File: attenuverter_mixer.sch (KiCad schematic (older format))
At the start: 98 parts, among them J0 Eurorack power, J1 Input, J10 Or out, J2 Out, J3 Input, J4 Out, J5 Input, J6 Input, J7 Out, J8 Out, J9 Sum out, U1 TL072, U2 TL072, U3 TL072, U4 TL072, U5 TL074, U6 LM4040CIZ-5.0

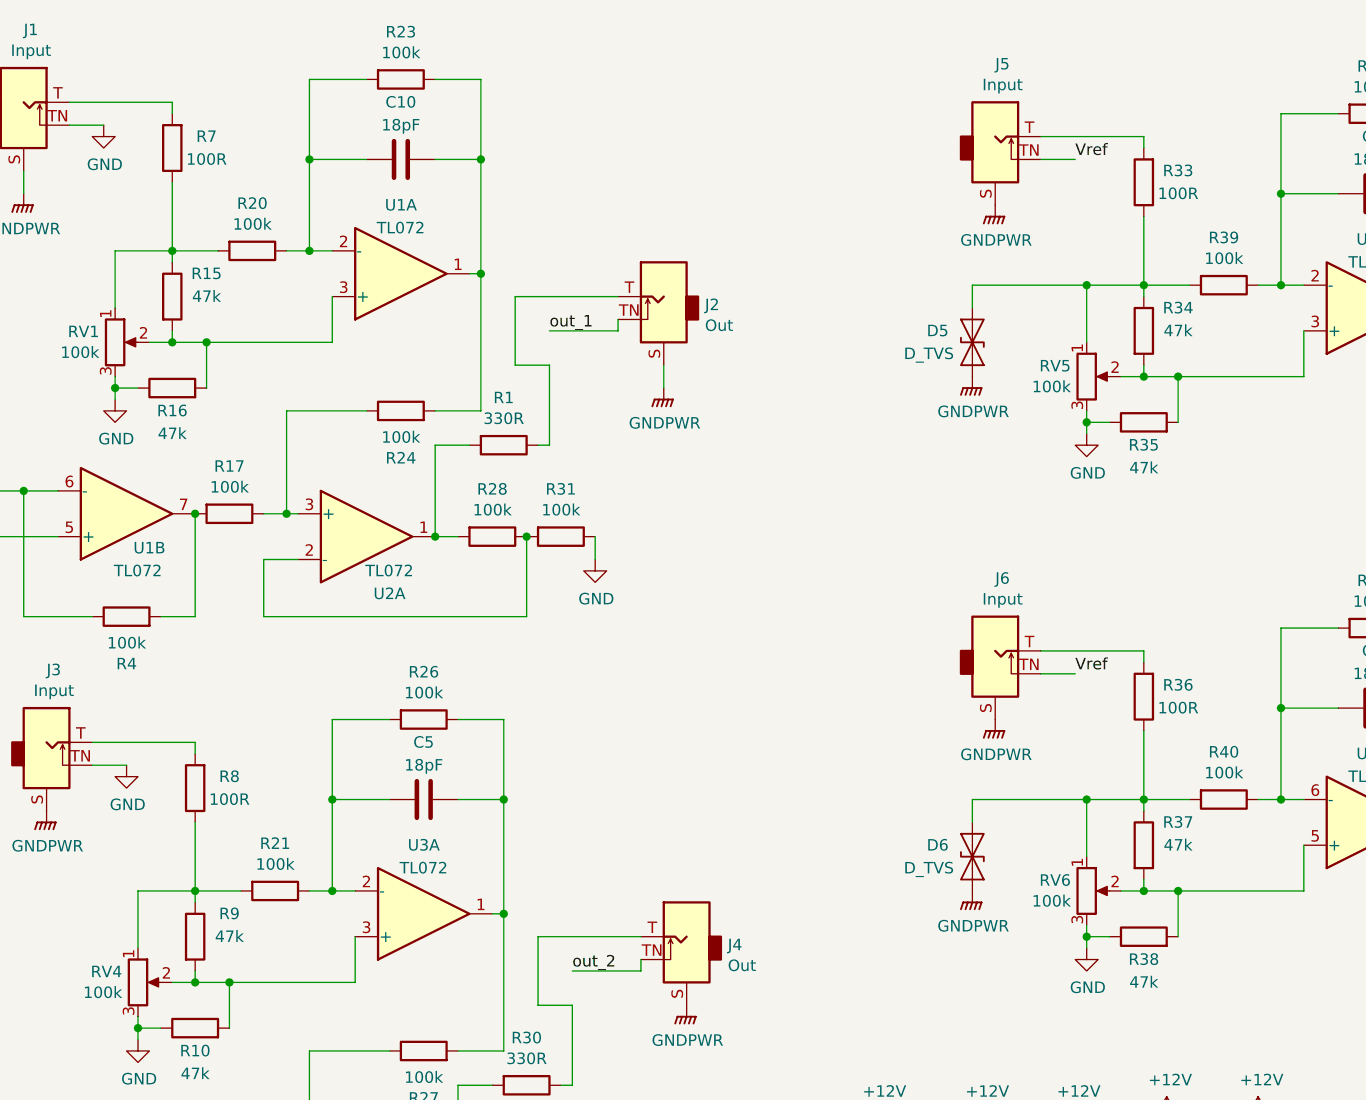
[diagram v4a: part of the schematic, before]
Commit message: remove two more TVS diodes; remove input resistors; use SM resistors
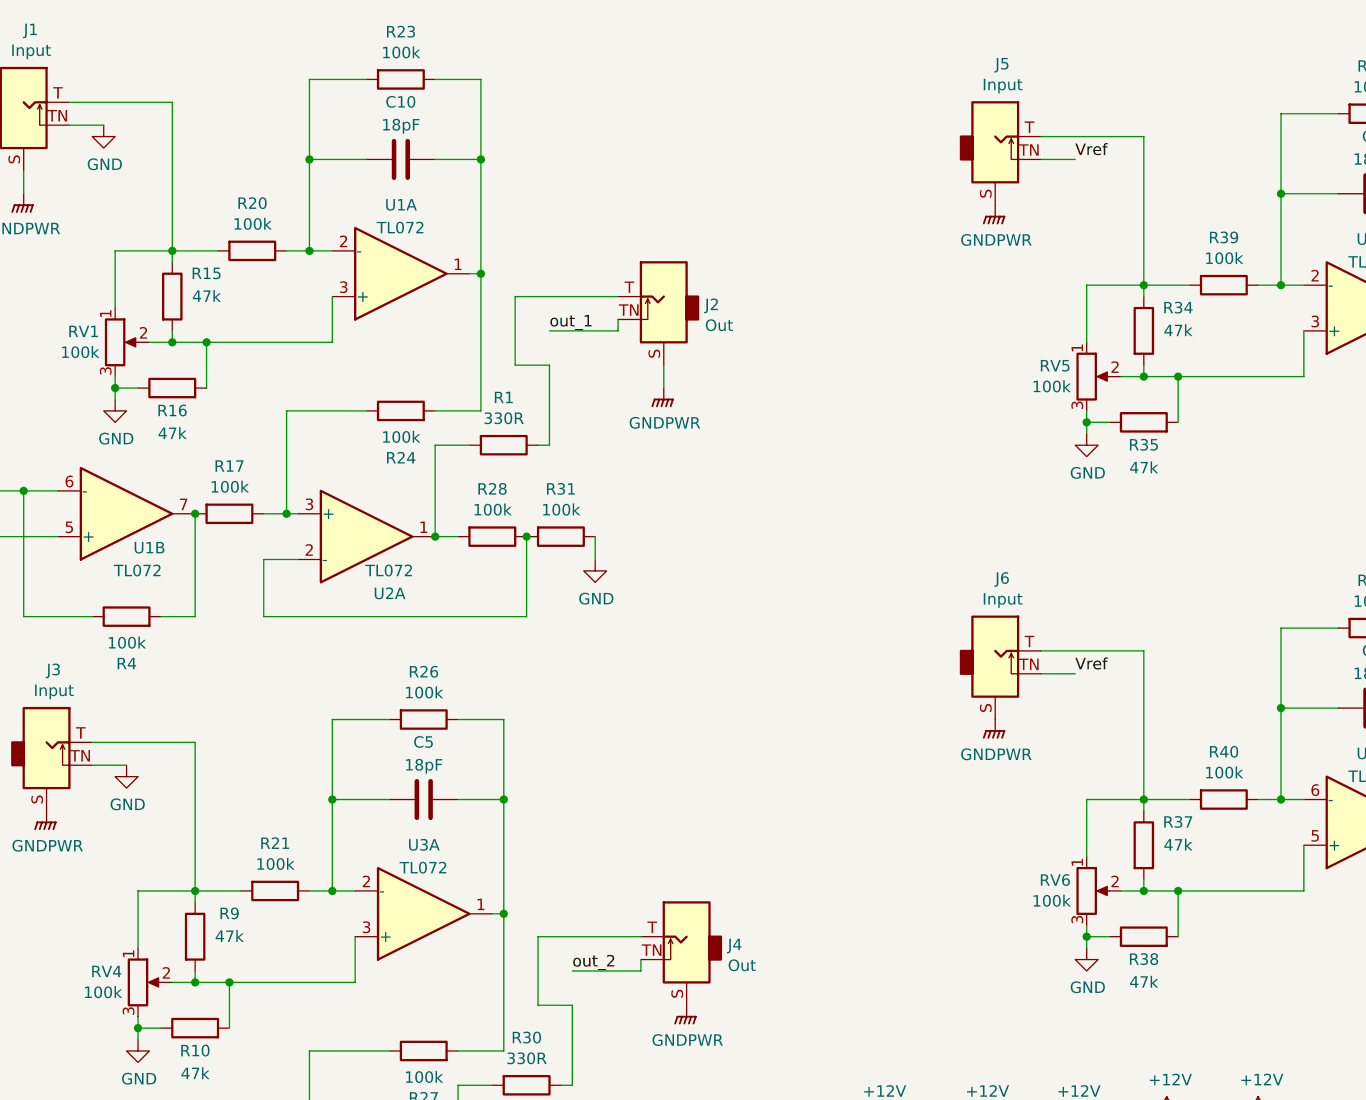
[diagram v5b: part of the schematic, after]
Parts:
- removed D5, D6: D_TVS, Diode_THT:D_DO-15_P12.70mm_Horizontal, symbol Device:D_TVS
- removed R33, R36, R7, R8: 100R, Resistor_THT:R_Axial_DIN0204_L3.6mm_D1.6mm_P7.62mm_Horizontal, symbol Device:R
- R10, R11, R12, R13, R14, R15, R16, R17, R18, R19, R2, R20, R21, R22, R23, R24, R25, R26, R27, R28, R29, R3, R34, R35, R37, R38, R39, R4, R40, R41, R42, R45, R46, R6, R9: footprint Resistor_THT:R_Axial_DIN0207_L6.3mm_D2.5mm_P10.16mm_Horizontal -> Resistor_SMD:R_1206_3216Metric_Pad1.42x1.75mm_HandSolder
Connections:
- net at J1.T: now also R15.1, R20.2, RV1.1
- net at J3.T: now also R21.2, R9.1, RV4.1
- net at J5.T: now also R34.1, R39.2, RV5.1
- net at J6.T: now also R37.1, R40.2, RV6.1

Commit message: Where it's at, just before changing the op amp configuration
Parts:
- J0: symbol Connector_Generic:Conn_02x05_Counter_Clockwise -> Connector_Generic:Conn_02x05_Odd_Even
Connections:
- net GND: now also J0.3 (Pin_3), J0.8 (Pin_8); no longer J0.2 (Pin_2), J0.9 (Pin_9)
- net GNDPWR: now also J0.5 (Pin_5), J0.6 (Pin_6); no longer J0.3 (Pin_3), J0.8 (Pin_8)
- net at D16.1 (K), J0.1 (Pin_1): now also J0.2 (Pin_2); no longer J0.10 (Pin_10)
- new net: D17.2 (A), J0.10 (Pin_10), J0.9 (Pin_9)
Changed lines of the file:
@@
 $EndComp
 $Comp
-L Connector_Generic:Conn_02x05_Counter_Clockwise J0
+L Connector_Generic:Conn_02x05_Odd_Even J0
 U 1 1 5DF894B6
 P 10050 1450

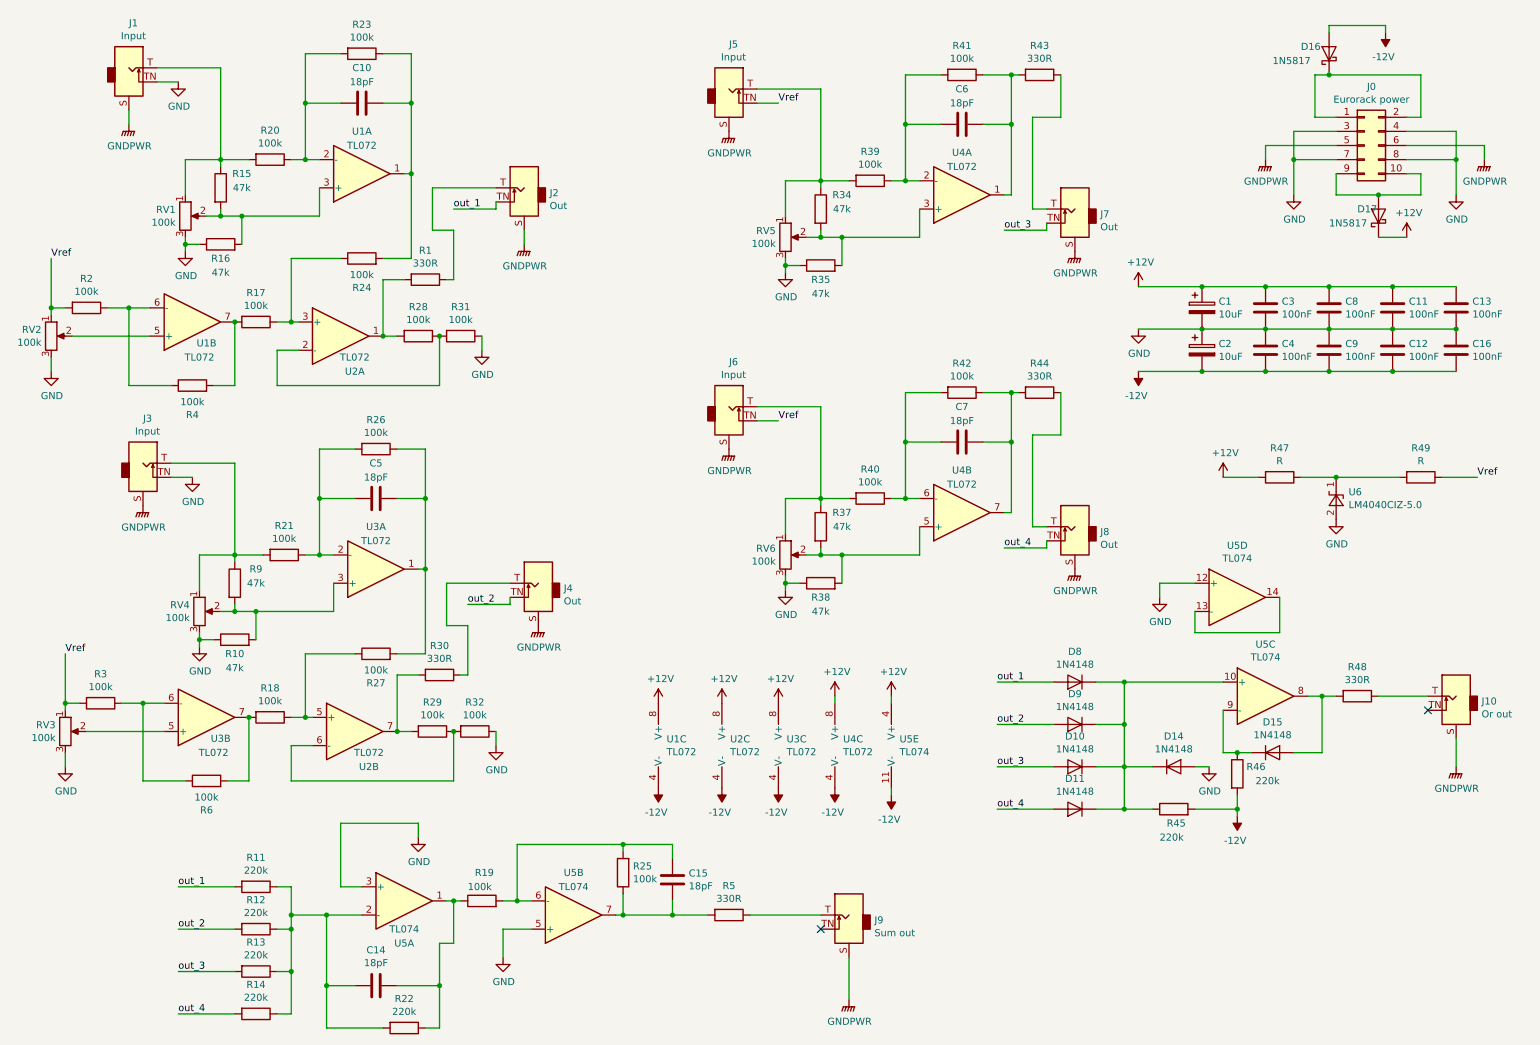
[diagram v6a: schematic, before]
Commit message: V01 as fabricated
- Use surface mount 100K and 220K to allow single board.
- Drop offset pots --- just have atteunuvert controls on each channel.
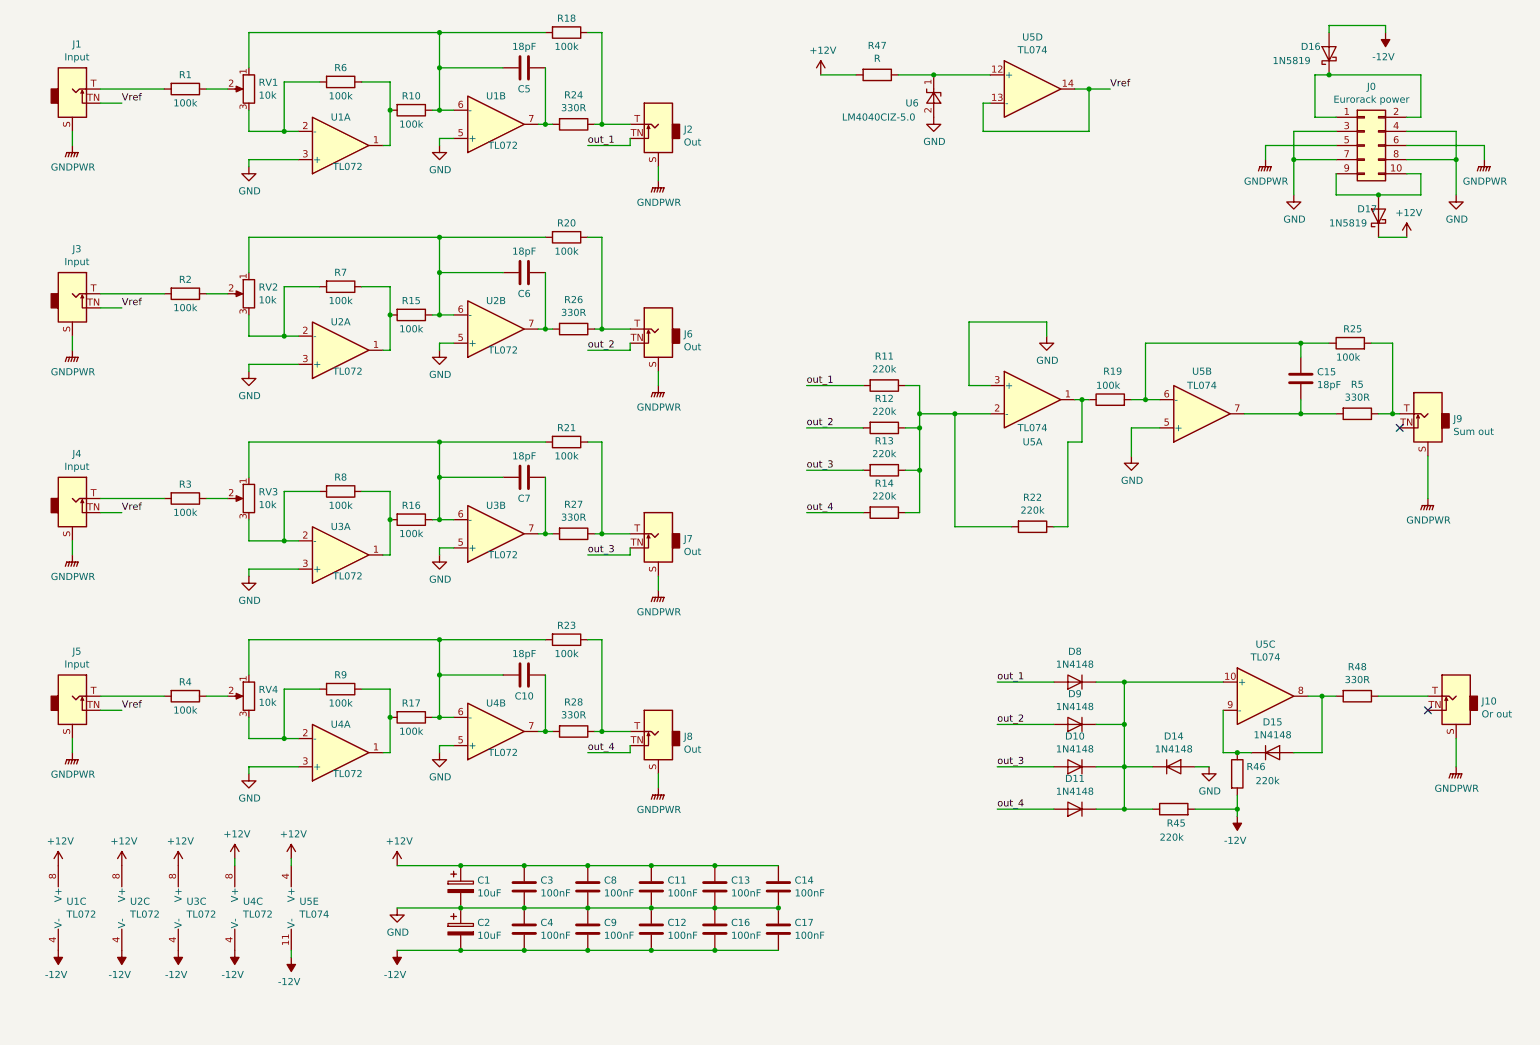
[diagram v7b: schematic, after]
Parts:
- removed R29, R39, R40, R41, R42: 100k, Resistor_SMD:R_1206_3216Metric_Pad1.42x1.75mm_HandSolder, symbol Device:R
- removed R30, R43, R44: 330R, Resistor_THT:R_Axial_DIN0309_L9.0mm_D3.2mm_P12.70mm_Horizontal, symbol Device:R
- removed R31, R32: 100k, Resistor_THT:R_Axial_DIN0207_L6.3mm_D2.5mm_P10.16mm_Horizontal, symbol Device:R
- removed R34, R35, R37, R38: 47k, Resistor_SMD:R_1206_3216Metric_Pad1.42x1.75mm_HandSolder, symbol Device:R
- removed R49: R, Resistor_THT:R_Axial_DIN0309_L9.0mm_D3.2mm_P12.70mm_Horizontal, symbol Device:R
- removed RV5, RV6: 100k, Potentiometer_THT:Potentiometer_Alpha_RD901F-40-00D_Single_Vertical, symbol Device:R_POT
- added C17: 100nF, Capacitor_THT:C_Disc_D3.0mm_W1.6mm_P2.50mm, symbol Device:C
- added R7, R8: 100k, Resistor_SMD:R_1206_3216Metric_Pad1.42x1.75mm_HandSolder, symbol Device:R
- C14: value 18pF -> 100nF; footprint Capacitor_THT:C_Disc_D3.0mm_W2.0mm_P2.50mm -> Capacitor_THT:C_Disc_D3.0mm_W1.6mm_P2.50mm
- D16, D17: value 1N5817 -> 1N5819
- J4: value Out -> Input
- J6: value Input -> Out
- R1: value 330R -> 100k; footprint Resistor_THT:R_Axial_DIN0309_L9.0mm_D3.2mm_P12.70mm_Horizontal -> Resistor_SMD:R_1206_3216Metric_Pad1.42x1.75mm_HandSolder
- R10, R15, R16, R9: value 47k -> 100k
- R24, R26, R27, R28: value 100k -> 330R; footprint Resistor_SMD:R_1206_3216Metric_Pad1.42x1.75mm_HandSolder -> Resistor_THT:R_Axial_DIN0309_L9.0mm_D3.2mm_P12.70mm_Horizontal
- R47, R48, R5: footprint Resistor_THT:R_Axial_DIN0309_L9.0mm_D3.2mm_P12.70mm_Horizontal -> Resistor_THT:R_Axial_DIN0309_L9.0mm_D3.2mm_P2.54mm_Vertical
- RV1, RV2, RV3, RV4: value 100k -> 10k
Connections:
- net +12V: now also C14.1
- net -12V: now also C17.2
- net GND: now also C14.2, U1.3 (+), U1.5 (+), U2.3 (+), U2.5 (+), U3.3 (+), U3.5 (+), U4.3 (+), U4.5 (+), C17.1; no longer J1.TN, J3.TN, R10.1, R16.1, RV1.3, RV2.3, RV3.3, RV4.3, U5.12 (+)
- net Vref: now also J1.TN, J3.TN, J4.TN, U5.13 (-), U5.14; no longer J6.TN, R2.2, R3.2, RV2.1, RV3.1
- net out_2: now also J6.TN; no longer J4.TN
- net at R15.1, R20.2: now also C6.2, RV2.1, U2.6 (-); no longer J1.T, RV1.1
- net at R47.1, U6.1 (K): now also U5.12 (+)
- net at J2.T: now also R18.1, R24.1; no longer R1.1
- net at R11.1, R12.1, R13.1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: no longer C14.2
- net at R19.1, R22.1, U5.1: no longer C14.1
- net at J4.T: now also R3.2
- net at U2.7: now also C6.1, R26.2
- net at RV3.2: now also R3.1; no longer U3.5 (+)
- net at J9.T, R5.1: now also R25.2
- net at C15.1, R5.2, U5.7: no longer R25.1
- net at C15.2, R19.2, U5.6 (-): now also R25.1; no longer R25.2
- net at J5.T: now also R4.2
- net at U4.2 (-): now also R9.2, RV4.3; no longer C6.1
- net at U4.1: now also R17.2, R9.1; no longer C6.2
- net at J7.T: now also R21.1, R27.1
- net at RV2.2: now also R2.1; no longer U1.5 (+)
- net at U2.2 (-): now also RV2.3, R7.2; no longer R28.1
- net at J6.T: now also R20.1, R26.1
- net at C7.1: now also R27.2, U3.7; no longer U4.6 (-)
- net at C7.2: now also R16.1, R21.2, RV3.1, U3.6 (-); no longer U4.7
- net at J8.T: now also R23.1, R28.1
- new net: J1.T, R1.2
- new net: R1.1, RV1.2
- new net: C5.2, R10.1, R18.2, RV1.1, U1.6 (-)
- new net: R6.2, RV1.3, U1.2 (-)
- new net: R10.2, R6.1, U1.1
- new net: C5.1, R24.2, U1.7
- new net: J3.T, R2.2
- new net: R15.2, R7.1, U2.1
- new net: R8.2, RV3.3, U3.2 (-)
- new net: R16.2, R8.1, U3.1
- new net: R4.1, RV4.2
- new net: C10.2, R17.1, R23.2, RV4.1, U4.6 (-)
- new net: C10.1, R28.2, U4.7
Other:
- moved on the sheet: C1, C11, C12, C13, C15, C16, C2, C3, C4, C8, C9, J1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
